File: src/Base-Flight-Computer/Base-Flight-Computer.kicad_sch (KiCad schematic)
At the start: 62 parts, among them J1 Jumper_NO, P1 1984659, P2 USB, P3 0530470610, P4 1984659, P5 1984659, Q1 QS5U17TR, Q2 2N7002W-7-F, Q3 2N7002W-7-F, Q4 QS5U17TR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

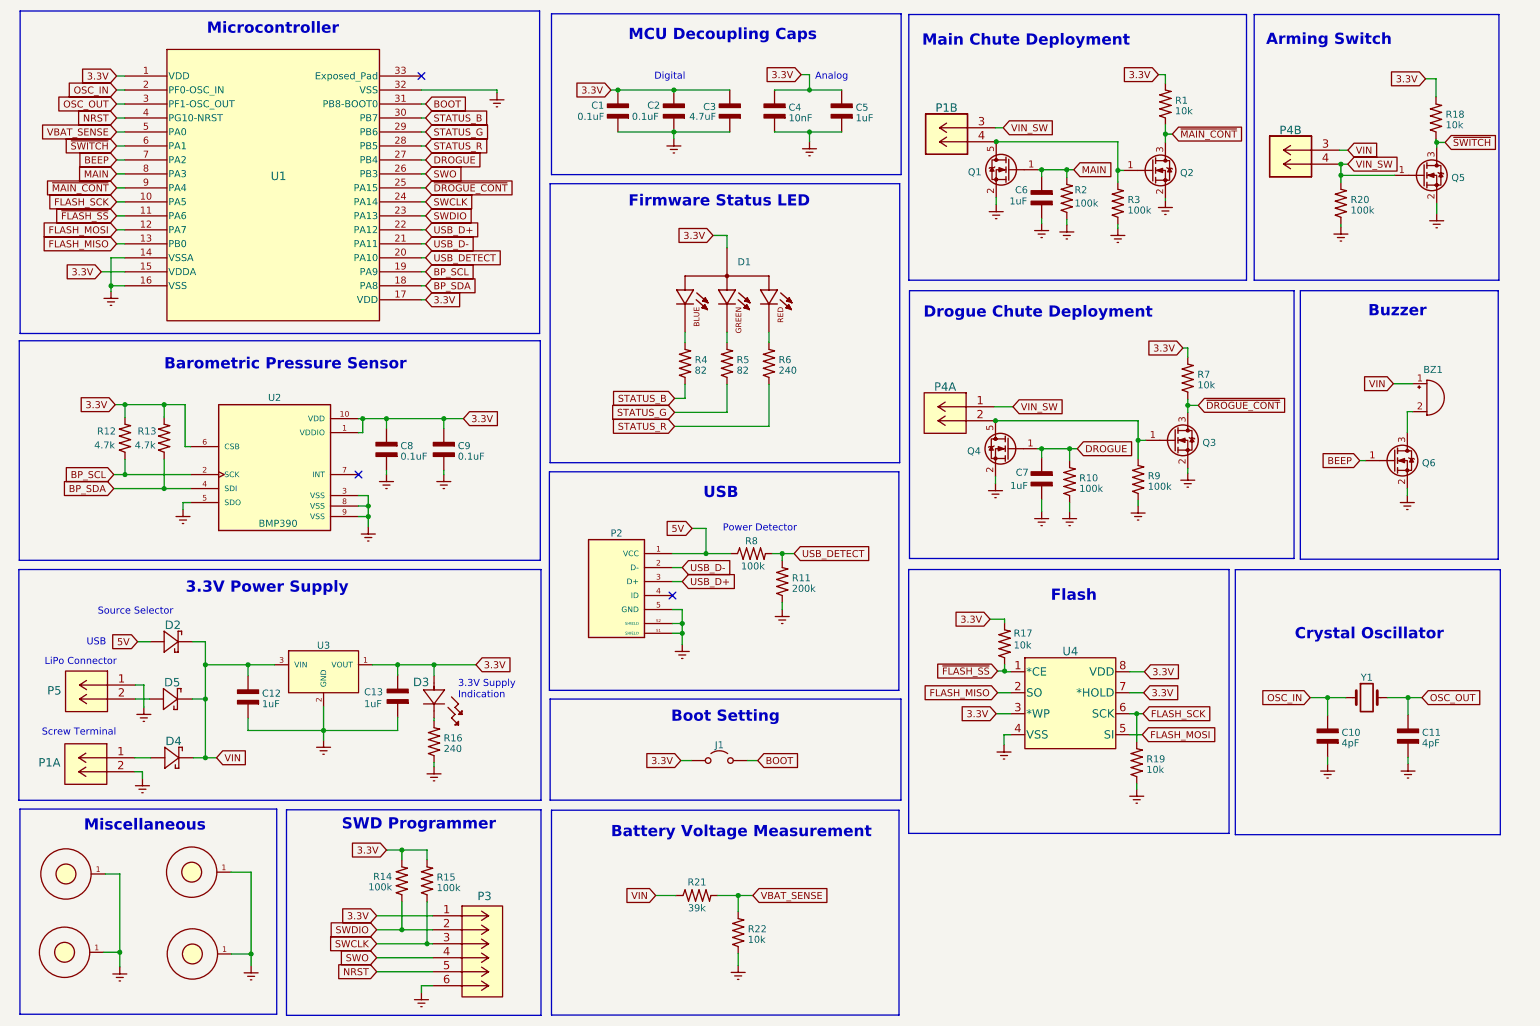
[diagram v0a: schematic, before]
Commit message: swapped out 90 degree LiPo connector for straight connector
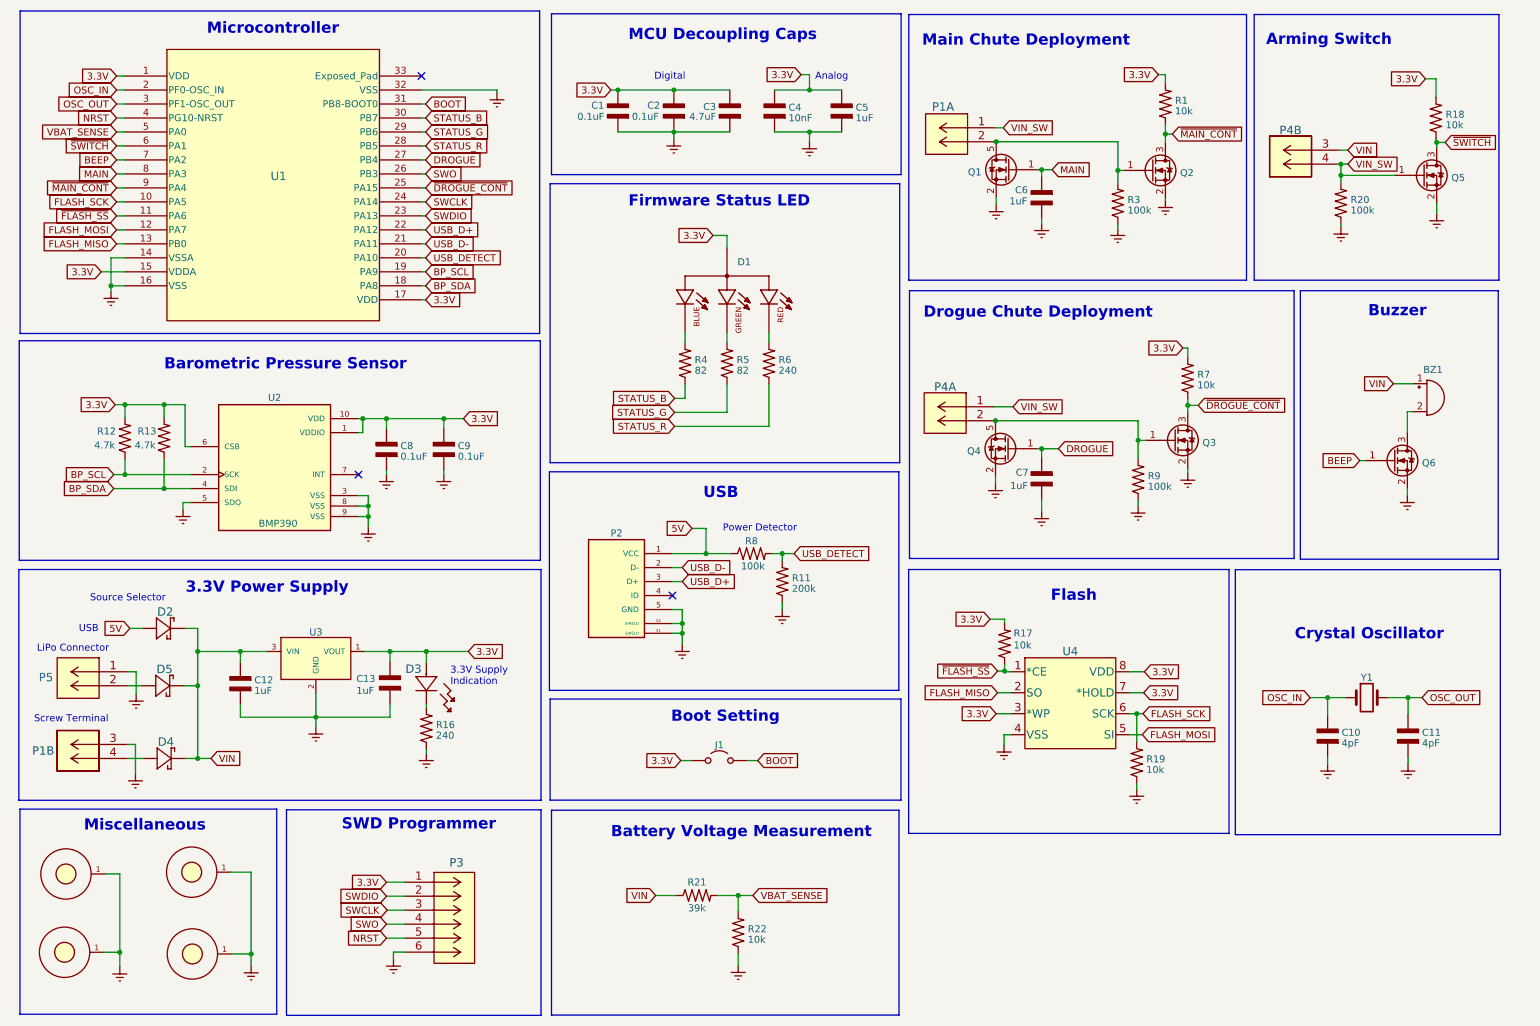
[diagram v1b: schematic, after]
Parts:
- removed P5: 1984659, Base-Flight-Computer:JST_S2B-PH-K-S(LF)(SN), symbol Base-Flight-Computer:S2B-PH-K-S__LF__SN
- removed R10, R14, R15, R2: 100k, Base-Flight-Computer:RES_0402, symbol Base-Flight-Computer:RES_0402
- added P5: B2B-PH-K-SLFSN_JST, Base-Flight-Computer:B2B-PH-K-SLFSN_JST, symbol Base-Flight-Computer:B2B-PH-K-SLFSN_JST
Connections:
- net Earth: now also P1.3 (5), P5.1 (5); no longer P1.2 (6)
- net VIN_SW: now also P1.1 (5); no longer P1.3 (5)
- net at Q1.5 (D), Q2.1 (G), R3.2: now also P1.2 (6); no longer P1.4 (6)
- net at D5.A: now also P5.2 (6)
- net at D4.A: now also P1.4 (6); no longer P1.1 (5)
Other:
- moved on the sheet: C12, C13, D2, D3, D4, D5, P1A, P1B, P3, R16, U3

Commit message: created new project for preliminary hardware testing
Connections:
- net Earth: now also U1.33 (Exposed_Pad)
- net STATUS_B: now also U1.9 (PA4); no longer U1.30 (PB7)
- net ~{MAIN_CONT}: now also U1.30 (PB7); no longer U1.9 (PA4)
- no-connect marks 3 -> 2
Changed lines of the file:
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@@
   (junction (at 144.399 174.117) (diameter 0) (color 0 0 0 0)
+  )
+  (junction (at 88.646 27.813) (diameter 0) (color 0 0 0 0)
   )
   (junction (at 40.132 100.203) (diameter 0) (color 0 0 0 0)
@@
   (no_connect (at 75.438 97.663))
   (no_connect (at 132.461 119.634))
-  (no_connect (at 86.868 25.273))
   (wire (pts (xy 86.868 53.213) (xy 87.63 53.213))
     (stroke (width 0) (type default))
@@
     (stroke (width 0) (type default))
   )
-  (wire (pts (xy 86.868 27.813) (xy 100.584 27.813))
+  (wire (pts (xy 86.868 27.813) (xy 88.646 27.813))
     (stroke (width 0) (type default))
   )
@@
     (stroke (width 0) (type default))
   )
+  (wire (pts (xy 86.868 25.273) (xy 88.646 25.273))
+    (stroke (width 0) (type default))
+  )
   (wire (pts (xy 86.868 30.353) (xy 87.63 30.353))
     (stroke (width 0) (type default))
@@
     (stroke (width 0) (type default))
   )
+  (wire (pts (xy 88.646 27.813) (xy 100.584 27.813))
+    (stroke (width 0) (type default))
+  )
   (wire (pts (xy 80.518 181.864) (xy 83.82 181.864))
     (stroke (width 0) (type default))
@@
     (stroke (width 0) (type default))
   )
+  (wire (pts (xy 31.496 45.593) (xy 33.02 45.593))
+    (stroke (width 0) (type default))
+  )
   (wire (pts (xy 216.789 153.797) (xy 216.789 154.813))
     (stroke (width 0) (type default))
@@
     (stroke (width 0) (type default))
   )
+  (wire (pts (xy 88.646 25.273) (xy 88.646 27.813))
+    (stroke (width 0) (type default))
+  )
   (wire (pts (xy 31.496 55.753) (xy 33.02 55.753))
     (stroke (width 0) (type default))
@@
   )
   (wire (pts (xy 46.228 129.794) (xy 46.228 125.603))
-    (stroke (width 0) (type default))
-  )
-  (wire (pts (xy 31.496 45.593) (xy 33.02 45.593))
     (stroke (width 0) (type default))
   )
@@
     )
   )
-  (global_label "~{MAIN_CONT}" (shape input) (at 31.496 45.593 180) (fields_autoplaced)
-    (effects (font (size 1.27 1.27)) (justify right))
-    (property "Intersheetrefs" "${INTERSHEET_REFS}" (at 18.7415 45.6724 0)
-      (effects (font (size 1.27 1.27)) (justify right) hide)
+  (global_label "~{MAIN_CONT}" (shape input) (at 87.63 32.893 0) (fields_autoplaced)
+    (effects (font (size 1.27 1.27)) (justify left))
+    (property "Intersheetrefs" "${INTERSHEET_REFS}" (at 100.3845 32.9724 0)
+      (effects (font (size 1.27 1.27)) (justify left) hide)
     )
   )
@@
     )
   )
-  (global_label "STATUS_B" (shape input) (at 87.63 32.893 0) (fields_autoplaced)
-    (effects (font (size 1.27 1.27)) (justify left))
-    (property "Intersheetrefs" "${INTERSHEET_REFS}" (at 99.0541 32.8136 0)
-      (effects (font (size 1.27 1.27)) (justify left) hide)
-    )
-  )
+  (global_label "STATUS_B" (shape input) (at 31.496 45.593 180) (fields_autoplaced)
+    (effects (font (size 1.27 1.27)) (justify right))
+    (property "Intersheetrefs" "${INTERSHEET_REFS}" (at 20.0719 45.5136 0)
+      (effects (font (size 1.27 1.27)) (justify right) hide)
+    )
+  )
